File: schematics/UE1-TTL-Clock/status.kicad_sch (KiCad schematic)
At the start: 40 parts

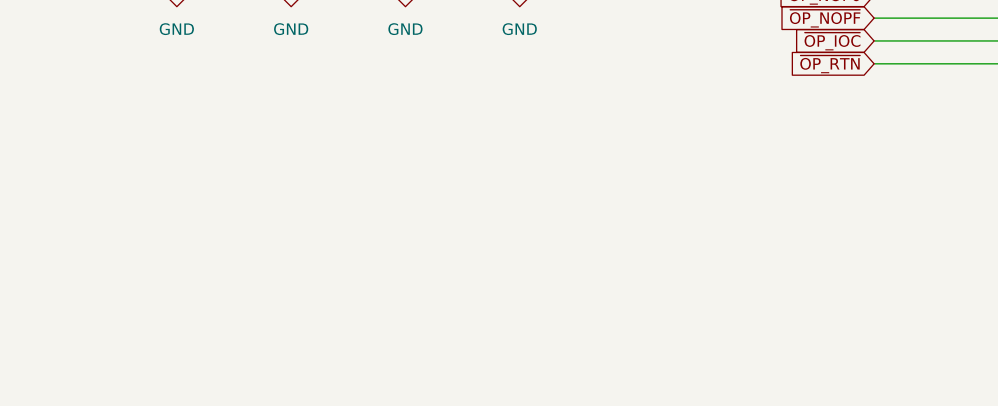
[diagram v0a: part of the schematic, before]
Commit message: Lay out clock board
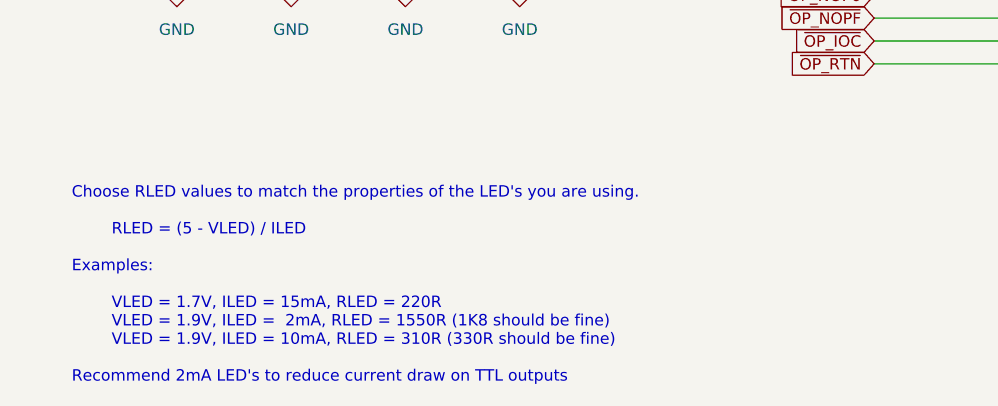
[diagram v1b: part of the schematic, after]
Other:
- note added: "Choose RLED values to match the properties of the LED's you are using. RLED = (5 - VLED) / ILED Examples: VLED = 1.7V, ILED = 15mA, RLED = 220R VLED = 1.9V, ILED = 2mA, RLED = 1550R (1K8 should be fine) VLED = 1.9V, ILED = 10mA, RLED = 310R (330R should be fine) Recommend 2mA LED's to reduce current draw on TTL outputs"
- title: UE1- TTL Clock and Diagnostics -> UE1-TTL Clock and Front Panel
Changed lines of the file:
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@@
 	(paper "A4")
 	(title_block
-		(title "UE1- TTL Clock and Diagnostics")
+		(title "UE1-TTL Clock and Front Panel")
 		(date "2025")
 		(rev "1")
@@
 		)
 	)
+	(text "Choose RLED values to match the properties of the LED's you are using.\n\n        RLED = (5 - VLED) / ILED\n\nExamples:\n\n        VLED = 1.7V, ILED = 15mA, RLED = 220R\n        VLED = 1.9V, ILED =  2mA, RLED = 1550R (1K8 should be fine)\n        VLED = 1.9V, ILED = 10mA, RLED = 310R (330R should be fine)\n\nRecommend 2mA LED's to reduce current draw on TTL outputs"
+		(exclude_from_sim no)
+		(at 41.656 174.498 0)
+		(effects
+			(font
+				(size 1.27 1.27)
+			)
+			(justify left)
+		)
+	)
